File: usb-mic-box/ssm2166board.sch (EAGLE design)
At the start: 23 parts, among them IC1 SSM2166S, X1 PG203J

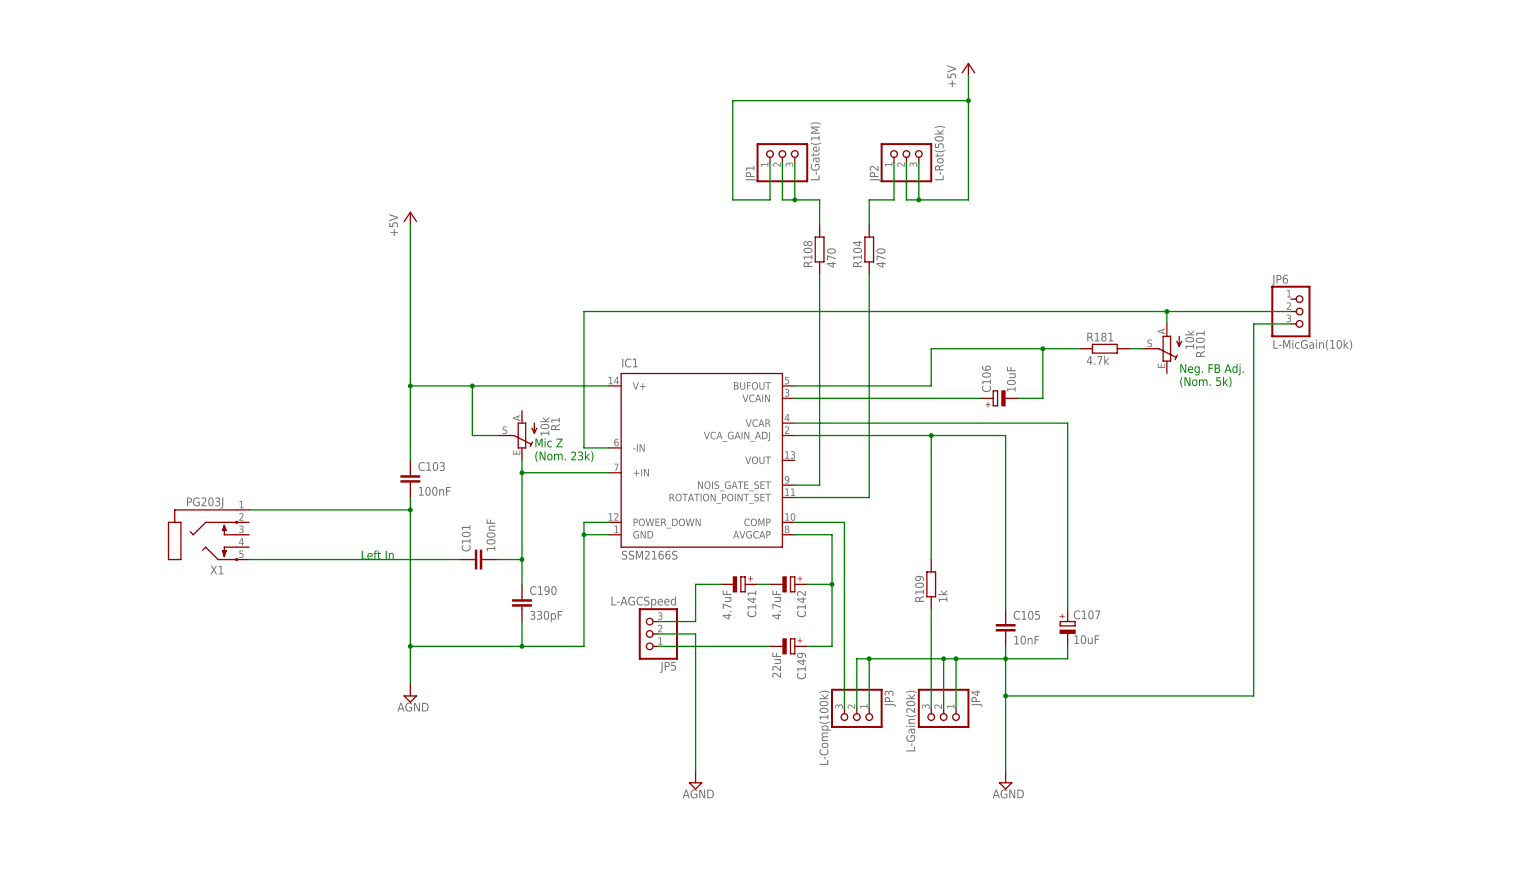
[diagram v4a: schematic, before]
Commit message: Some corrections to SSM2166 schematic, and filling in more missing stuff
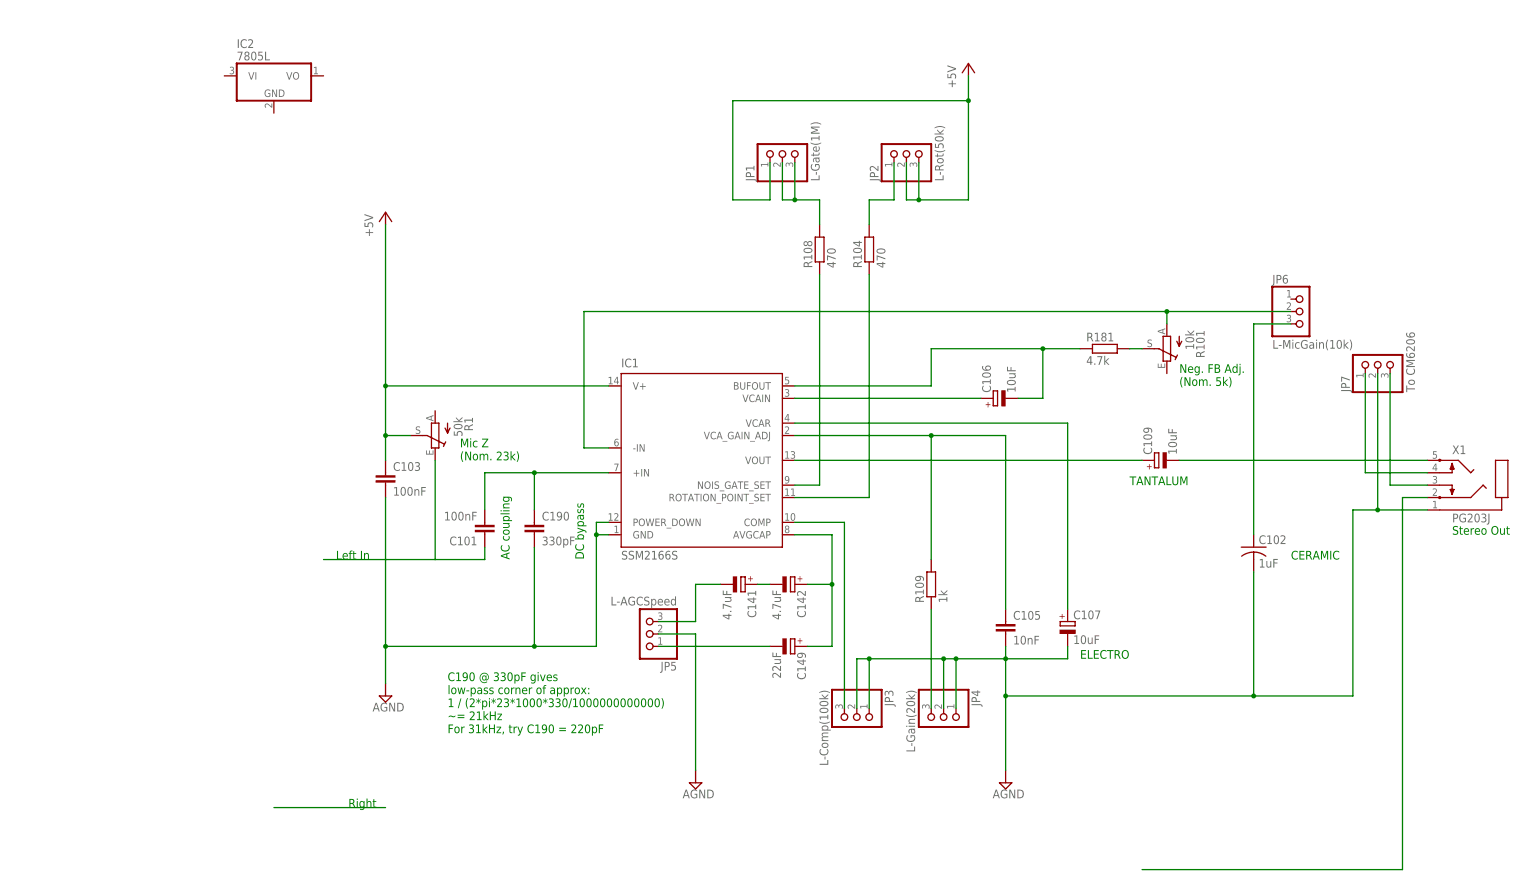
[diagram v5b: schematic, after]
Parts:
- added C102: 1uF, resistor:C-USC2220K
- added C109: 10uF, resistor:CPOL-EUCT6032
- added IC2: 7805L, linear:7805L
- added JP7: To CM6206, anton:PINHD-1X3
- R1: value 10k -> 50k
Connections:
- new net N$19: C102.1, JP6.3
- new net N$20: C109.+, IC1.VOUT
- new net N$21: C109.-, X1.5
- new net N$22: C101.1, R1.E
- new net N$24: JP7.3, X1.3
- new net N$25: X1.2
- net AGND: now also C102.2, JP7.2; no longer JP6.3
- net N$12: now also JP7.1, X1.4; no longer C101.1, X1.5
- net N$3: no longer R1.E
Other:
- note added: "AC coupling"
- note added: "C190 @ 330pF gives low-pass corner of approx: 1 / (2*pi*23*1000*330/1000000000000) ~= 21kHz For 31kHz, try C190 = 220pF"
- note added: "CERAMIC"
- note added: "DC bypass"
- note added: "ELECTRO"
- note added: "Right"
- note added: "Stereo Out"
- note added: "TANTALUM"
- moved on the sheet: C101, C103, C190, R1, X1

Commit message: Added voltage regulator and USB passthru to SSM2166 board schematics
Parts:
- added C1: 100uF, rcl:CPOL-EUE2-5
- added C2: 10uF, rcl:CPOL-EUE2-5
- added D1: 1N4004, diode:1N4004
- added J1: 9VDC, con-jack:DCJ0303
- added JP8: (no value), anton:PINHD-1X4
- added X2: PN61729-S, con-berg:PN61729-S
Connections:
- new net GND: C1.-, C2.-, IC2.GND, J1.1
- new net N$26: JP8.1, X2.1
- new net N$27: JP8.2, X2.2
- new net N$28: JP8.3, X2.3
- new net N$29: JP8.4, X2.4, X2.S1, X2.S2
- new net N$30: C1.+, D1.C, IC2.VI
- new net N$33: D1.A, J1.3
- net +5V: now also C2.+, IC2.VO
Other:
- note added: "+5V"
- note added: "+D"
- note added: "-D"
- note added: "GND"
- note added: "Left Out"
- note added: "Right Out"
- note added: "TANTALUMS"
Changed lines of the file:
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@@
 <part name="IC2" library="linear" deviceset="78*" device="L" technology="05"/>
 <part name="JP7" library="anton" deviceset="PINHD-1X3" device="" value="To CM6206"/>
+<part name="X2" library="con-berg" deviceset="PN61729-S" device=""/>
+<part name="JP8" library="anton" deviceset="PINHD-1X4" device=""/>
+<part name="D1" library="diode" deviceset="1N4004" device=""/>
+<part name="C1" library="rcl" deviceset="CPOL-EU" device="E2-5" value="100uF"/>
+<part name="C2" library="rcl" deviceset="CPOL-EU" device="E2-5" value="10uF"/>
+<part name="J1" library="con-jack" deviceset="DCJ0303" device="" value="9VDC"/>
+<part name="SUPPLY4" library="supply2" deviceset="GND" device=""/>
+<part name="P+3" library="supply1" deviceset="+5V" device=""/>
 </parts>
 <sheets>
@@
 <text x="-15.24" y="17.78" size="1.778" layer="91">Right</text>
 <text x="210.82" y="73.66" size="1.778" layer="91">Stereo Out</text>
+<text x="180.34" y="88.9" size="1.778" layer="91">Left Out</text>
+<text x="180.34" y="5.08" size="1.778" layer="91">Right Out</text>
+<text x="195.58" y="165.1" size="1.778" layer="91">+5V</text>
+<text x="195.58" y="162.56" size="1.778" layer="91">-D</text>
+<text x="195.58" y="160.02" size="1.778" layer="91">+D</text>
+<text x="195.58" y="157.48" size="1.778" layer="91">GND</text>
+<text x="63.5" y="53.34" size="1.778" layer="91">TANTALUMS</text>
 </plain>
 <instances>
@@
 <instance part="IC2" gate="A1" x="-30.48" y="167.64"/>
 <instance part="JP7" gate="A" x="195.58" y="109.22" rot="R90"/>
+<instance part="X2" gate="G$1" x="205.74" y="160.02"/>
+<instance part="JP8" gate="A" x="170.18" y="160.02" rot="MR0"/>
+<instance part="D1" gate="1" x="-58.42" y="167.64"/>
+<instance part="C1" gate="G$1" x="-45.72" y="160.02"/>
+<instance part="C2" gate="G$1" x="-15.24" y="160.02"/>
+<instance part="J1" gate="G$1" x="-81.28" y="165.1"/>
+<instance part="SUPPLY4" gate="GND" x="-68.58" y="139.7"/>
+<instance part="P+3" gate="1" x="-2.54" y="180.34"/>
 </instances>
 <busses>
@@
 <junction x="101.6" y="142.24"/>
 <junction x="111.76" y="162.56"/>
+</segment>
+<segment>
+<pinref part="IC2" gate="A1" pin="VO"/>
+<pinref part="C2" gate="G$1" pin="+"/>
+<wire x1="-20.32" y1="167.64" x2="-15.24" y2="167.64" width="0.1524" layer="91"/>
+<wire x1="-15.24" y1="167.64" x2="-15.24" y2="162.56" width="0.1524" layer="91"/>
+<pinref part="P+3" gate="1" pin="+5V"/>
+<wire x1="-15.24" y1="167.64" x2="-2.54" y2="167.64" width="0.1524" layer="91"/>
+<wire x1="-2.54" y1="167.64" x2="-2.54" y2="177.8" width="0.1524" layer="91"/>
+<junction x="-15.24" y="167.64"/>
 </segment>
 </net>
@@
 </segment>
 </net>
+<net name="N$26" class="0">
+<segment>
+<pinref part="JP8" gate="A" pin="1"/>
+<pinref part="X2" gate="G$1" pin="1"/>
+<wire x1="172.72" y1="165.1" x2="203.2" y2="165.1" width="0.1524" layer="91"/>
+</segment>
+</net>
+<net name="N$27" class="0">
+<segment>
+<pinref part="X2" gate="G$1" pin="2"/>
+<pinref part="JP8" gate="A" pin="2"/>
+<wire x1="203.2" y1="162.56" x2="172.72" y2="162.56" width="0.1524" layer="91"/>
+</segment>
+</net>
+<net name="N$28" class="0">
+<segment>
+<pinref part="JP8" gate="A" pin="3"/>
+<pinref part="X2" gate="G$1" pin="3"/>
+<wire x1="172.72" y1="160.02" x2="203.2" y2="160.02" width="0.1524" layer="91"/>
+</segment>
+</net>
+<net name="N$29" class="0">
+<segment>
+<pinref part="X2" gate="G$1" pin="4"/>
+<pinref part="JP8" gate="A" pin="4"/>
+<wire x1="203.2" y1="157.48" x2="187.96" y2="157.48" width="0.1524" layer="91"/>
+<pinref part="X2" gate="G$1" pin="S1"/>
+<wire x1="187.96" y1="157.48" x2="172.72" y2="157.48" width="0.1524" layer="91"/>
+<wire x1="205.74" y1="152.4" x2="187.96" y2="152.4" width="0.1524" layer="91"/>
+<wire x1="187.96" y1="152.4" x2="187.96" y2="157.48" width="0.1524" layer="91"/>
+<pinref part="X2" gate="G$1" pin="S2"/>
+<wire x1="205.74" y1="149.86" x2="187.96" y2="149.86" width="0.1524" layer="91"/>
+<wire x1="187.96" y1="149.86" x2="187.96" y2="152.4" width="0.1524" layer="91"/>
+<junction x="187.96" y="152.4"/>
+<junction x="187.96" y="157.48"/>
+</segment>
+</net>
+<net name="N$30" class="0">
+<segment>
+<pinref part="D1" gate="1" pin="C"/>
+<pinref part="IC2" gate="A1" pin="VI"/>
+<wire x1="-55.88" y1="167.64" x2="-45.72" y2="167.64" width="0.1524" layer="91"/>
+<pinref part="C1" gate="G$1" pin="+"/>
+<wire x1="-45.72" y1="167.64" x2="-40.64" y2="167.64" width="0.1524" layer="91"/>
+<wire x1="-45.72" y1="162.56" x2="-45.72" y2="167.64" width="0.1524" layer="91"/>
+</segment>
+</net>
+<net name="N$33" class="0">
+<segment>
+<pinref part="J1" gate="G$1" pin="3"/>
+<wire x1="-73.66" y1="162.56" x2="-63.5" y2="162.56" width="0.1524" layer="91"/>
+<wire x1="-63.5" y1="162.56" x2="-63.5" y2="167.64" width="0.1524" layer="91"/>
+<pinref part="D1" gate="1" pin="A"/>
+<wire x1="-63.5" y1="167.64" x2="-60.96" y2="167.64" width="0.1524" layer="91"/>
+</segment>
+</net>
+<net name="GND" class="0">
+<segment>
+<pinref part="C1" gate="G$1" pin="-"/>
+<wire x1="-45.72" y1="154.94" x2="-45.72" y2="149.86" width="0.1524" layer="91"/>
+<wire x1="-45.72" y1="149.86" x2="-30.48" y2="149.86" width="0.1524" layer="91"/>
+<pinref part="IC2" gate="A1" pin="GND"/>
+<wire x1="-30.48" y1="149.86" x2="-30.48" y2="160.02" width="0.1524" layer="91"/>
+<pinref part="C2" gate="G$1" pin="-"/>
+<wire x1="-30.48" y1="149.86" x2="-15.24" y2="149.86" width="0.1524" layer="91"/>
+<wire x1="-15.24" y1="149.86" x2="-15.24" y2="154.94" width="0.1524" layer="91"/>
+<pinref part="J1" gate="G$1" pin="1"/>
+<wire x1="-73.66" y1="167.64" x2="-68.58" y2="167.64" width="0.1524" layer="91"/>
+<wire x1="-68.58" y1="167.64" x2="-68.58" y2="149.86" width="0.1524" layer="91"/>
+<wire x1="-68.58" y1="149.86" x2="-45.72" y2="149.86" width="0.1524" layer="91"/>
+<pinref part="SUPPLY4" gate="GND" pin="GND"/>
+<wire x1="-68.58" y1="142.24" x2="-68.58" y2="149.86" width="0.1524" layer="91"/>
+<junction x="-68.58" y="149.86"/>
+<junction x="-45.72" y="149.86"/>
+<junction x="-30.48" y="149.86"/>
+</segment>
+</net>
